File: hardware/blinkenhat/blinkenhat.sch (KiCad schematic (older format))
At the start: 26 parts, among them J1 LED1, J2 LED2, J3 INPUT, J4 Programmer, J5 USB_POWER, J6 GPIO, Q1 2N7002, Q2 2N7002, SW1 RESET, U1 AMS1117-3V3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

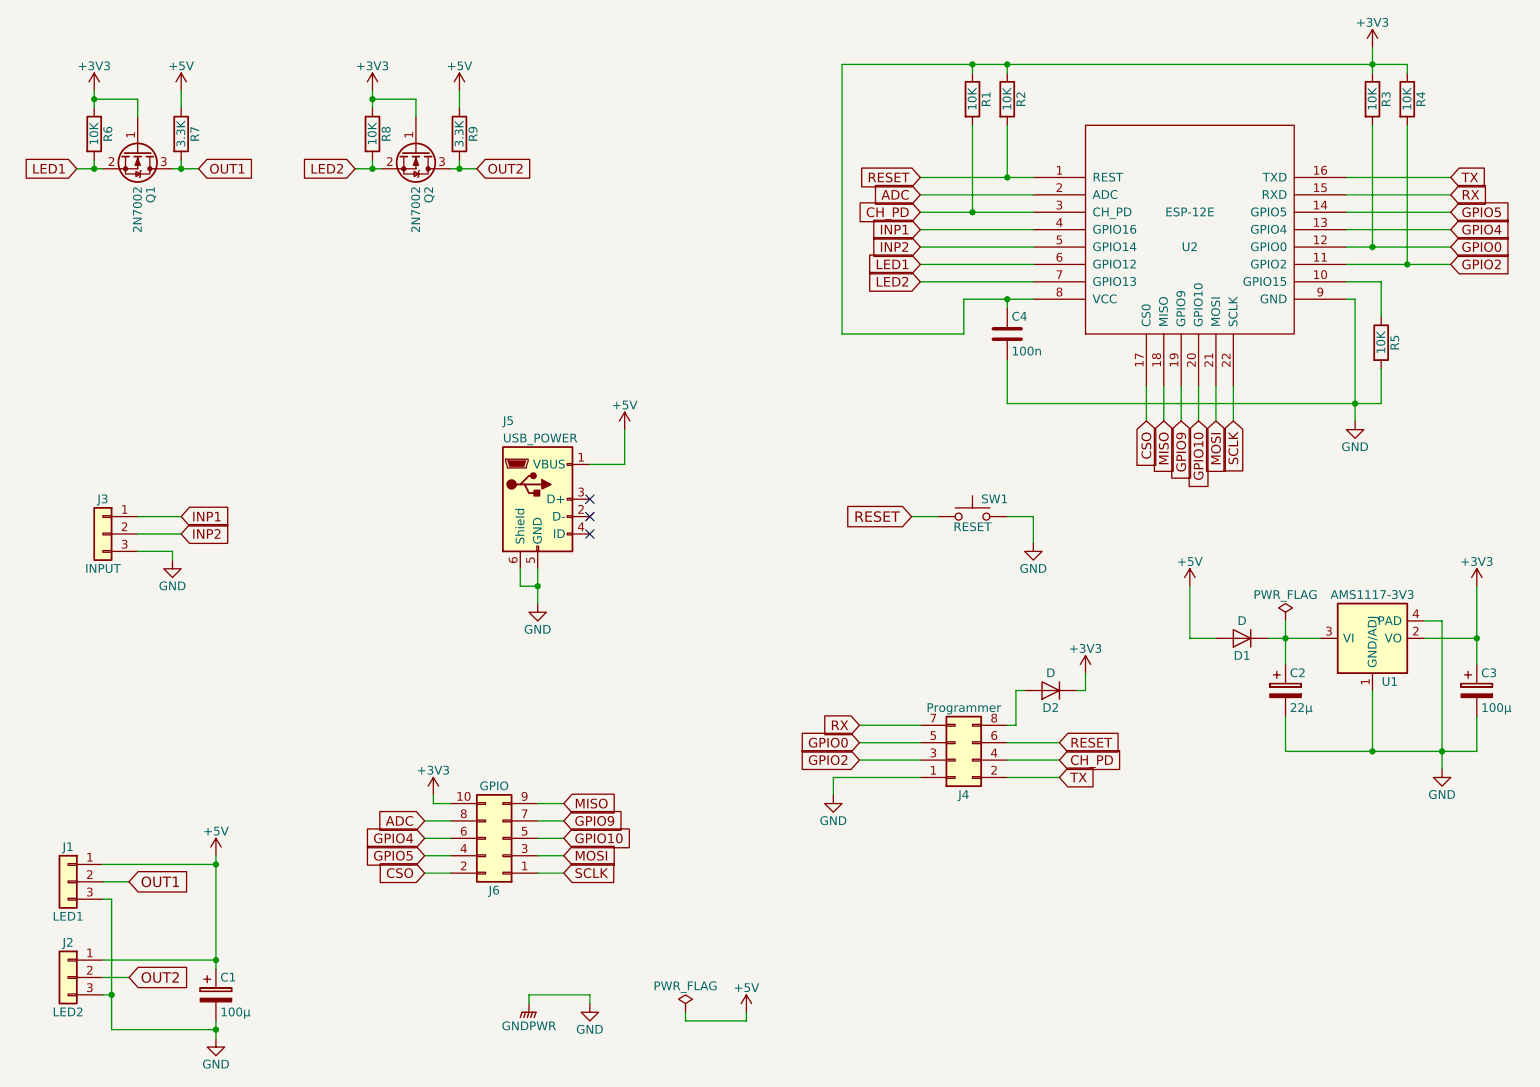
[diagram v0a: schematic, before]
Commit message: Hardware: another schematics update.
Signed-off-by: Jan Losinski <losinski@wh2.tu-dresden.de>
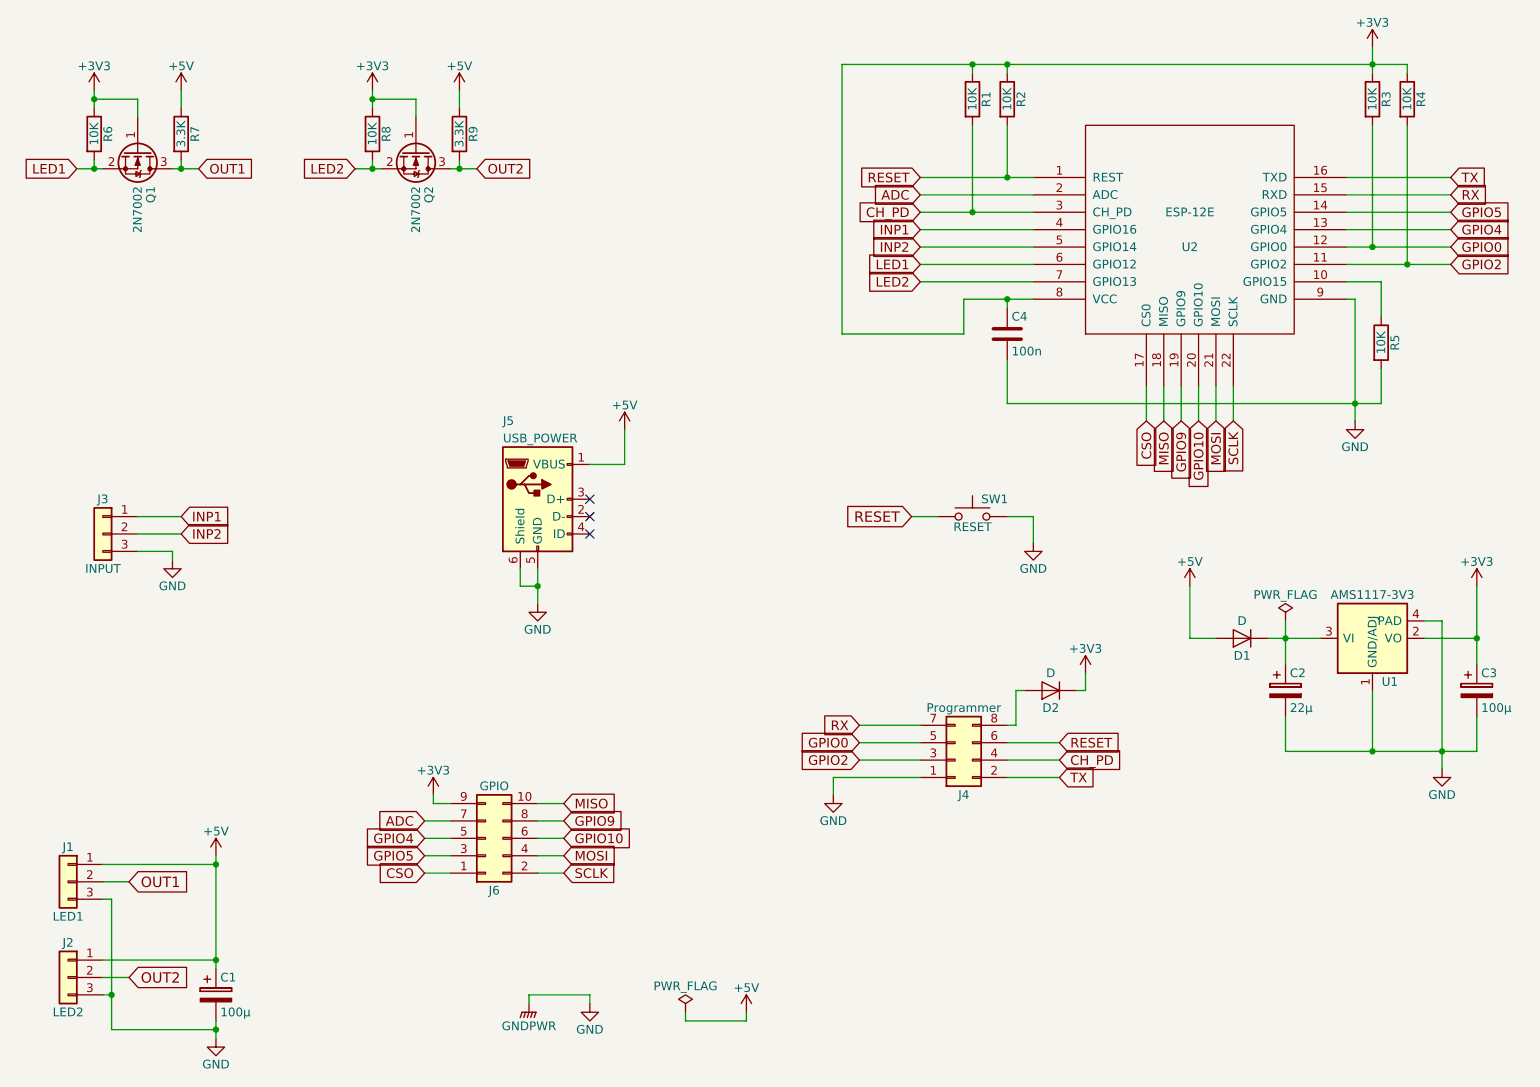
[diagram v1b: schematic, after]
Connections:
- net +3V3: now also J6.9 (Pin_9); no longer J6.10 (Pin_10)
- net ADC: now also J6.7 (Pin_7); no longer J6.8 (Pin_8)
- net CSO: now also J6.1 (Pin_1); no longer J6.2 (Pin_2)
- net GPIO10: now also J6.6 (Pin_6); no longer J6.5 (Pin_5)
- net GPIO4: now also J6.5 (Pin_5); no longer J6.6 (Pin_6)
- net GPIO5: now also J6.3 (Pin_3); no longer J6.4 (Pin_4)
- net GPIO9: now also J6.8 (Pin_8); no longer J6.7 (Pin_7)
- net MISO: now also J6.10 (Pin_10); no longer J6.9 (Pin_9)
- net MOSI: now also J6.4 (Pin_4); no longer J6.3 (Pin_3)
- net SCLK: now also J6.2 (Pin_2); no longer J6.1 (Pin_1)
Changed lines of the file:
@@
 L Conn_02x05_Odd_Even J6
 U 1 1 5A4EBCE1
-P 4300 6000
-F 0 "J6" H 4350 6300 50  0000 C CNN
-F 1 "GPIO" H 4350 5700 50  0000 C CNN
-F 2 "Pin_Headers:Pin_Header_Straight_2x05_Pitch1.27mm" H 4300 6000 50  0001 C CNN
-F 3 "" H 4300 6000 50  0001 C CNN
-	1    4300 6000
-	-1   0    0    1
+P 4200 6000
+F 0 "J6" H 4250 6300 50  0000 C CNN
+F 1 "GPIO" H 4250 5700 50  0000 C CNN
+F 2 "Pin_Headers:Pin_Header_Straight_2x05_Pitch1.27mm" H 4200 6000 50  0001 C CNN
+F 3 "" H 4200 6000 50  0001 C CNN
+	1    4200 6000
+	1    0    0    1
 $EndComp
 Text GLabel 6700 2300 0    55   Input ~ 0
@@
 	9300 5150 9300 5500
 Wire Wire Line
-	9900 4550 9900 5000
+	9900 4550 9900 4850
+Wire Wire Line
+	9900 4850 9900 5000
 Wire Wire Line
 	9900 4850 9600 4850
@@
 	9600 4750 9700 4750
 Wire Wire Line
-	9700 4750 9700 5600
+	9700 4750 9700 5500
+Wire Wire Line
+	9700 5500 9700 5600
 Connection ~ 9300 5500
 Wire Wire Line
 	8800 5300 8800 5500
 Wire Wire Line
-	8800 5500 9900 5500
+	8800 5500 9300 5500
+Wire Wire Line
+	9300 5500 9700 5500
+Wire Wire Line
+	9700 5500 9900 5500
 Connection ~ 8800 4850
 Wire Wire Line
@@
 Connection ~ 9900 4850
 Wire Wire Line
-	4500 4450 4500 4650
+	4500 4450 4500 4550
+Wire Wire Line
+	4500 4550 4500 4650
 Wire Wire Line
 	4500 4550 4400 4550
@@
 	7250 5350 7200 5350
 Wire Wire Line
-	9150 2600 9750 2600
+	9150 2600 9300 2600
+Wire Wire Line
+	9300 2600 9750 2600
 Wire Wire Line
 	9300 2600 9300 1900
@@
 	9500 1900 9500 2700
 Wire Wire Line
-	9150 2700 9750 2700
+	9150 2700 9500 2700
+Wire Wire Line
+	9500 2700 9750 2700
 Wire Wire Line
 	9150 2800 9350 2800
@@
 	9150 2900 9200 2900
 Wire Wire Line
-	9200 2900 9200 3600
+	9200 2900 9200 3500
+Wire Wire Line
+	9200 3500 9200 3600
 Wire Wire Line
 	9350 3500 9350 3300
@@
 	7200 1900 7200 2200
 Wire Wire Line
-	6700 2200 7350 2200
+	6700 2200 7200 2200
+Wire Wire Line
+	7200 2200 7350 2200
 Wire Wire Line
 	7000 1900 7000 2400
 Wire Wire Line
-	6700 2400 7350 2400
+	6700 2400 7000 2400
+Wire Wire Line
+	7000 2400 7350 2400
 Wire Wire Line
 	7000 1600 7000 1550
 Wire Wire Line
-	6250 1550 9500 1550
+	6250 1550 7000 1550
+Wire Wire Line
+	7000 1550 7200 1550
+Wire Wire Line
+	7200 1550 9300 1550
+Wire Wire Line
+	9300 1550 9500 1550
 Wire Wire Line
 	7200 1550 7200 1600
@@
 	6700 2800 7350 2800
 Wire Wire Line
-	6950 2900 7350 2900
+	6950 2900 7200 2900
+Wire Wire Line
+	7200 2900 7350 2900
 Wire Wire Line
 	6950 2900 6950 3100
@@
 	6250 3100 6250 1550
 Wire Wire Line
-	9300 1450 9300 1600
+	9300 1450 9300 1550
+Wire Wire Line
+	9300 1550 9300 1600
 Connection ~ 7200 1550
 Wire Wire Line
@@
 Connection ~ 9300 1550
 Wire Wire Line
-	7200 3500 9350 3500
+	7200 3500 9200 3500
+Wire Wire Line
+	9200 3500 9350 3500
 Wire Wire Line
 	7200 3500 7200 3250
@@
 	2000 6350 2050 6350
 Wire Wire Line
-	2050 6350 2050 7100
-Wire Wire Line
-	2650 6100 2650 6750
+	2050 6350 2050 6900
+Wire Wire Line
+	2050 6900 2050 7100
+Wire Wire Line
+	2650 6100 2650 6150
+Wire Wire Line
+	2650 6150 2650 6700
+Wire Wire Line
+	2650 6700 2650 6750
 Connection ~ 2650 6700
 Wire Wire Line
 	2050 7100 2650 7100
 Wire Wire Line
-	2650 7050 2650 7150
+	2650 7050 2650 7100
+Wire Wire Line
+	2650 7100 2650 7150
 Connection ~ 2050 6900
 Wire Wire Line
@@
 	3550 2100 3550 2150
 Wire Wire Line
-	3450 2150 3600 2150
-Wire Wire Line
-	4000 2150 4150 2150
+	3450 2150 3550 2150
+Wire Wire Line
+	3550 2150 3600 2150
+Wire Wire Line
+	4000 2150 4050 2150
+Wire Wire Line
+	4050 2150 4150 2150
 Wire Wire Line
 	4050 2150 4050 2100
 Wire Wire Line
-	2400 2150 2550 2150
+	2400 2150 2450 2150
+Wire Wire Line
+	2450 2150 2550 2150
 Wire Wire Line
 	2450 2150 2450 2100
@@
 	1950 2100 1950 2150
 Wire Wire Line
-	1850 2150 2000 2150
+	1850 2150 1950 2150
+Wire Wire Line
+	1950 2150 2000 2150
 Wire Wire Line
 	2200 1850 2200 1750
@@
 	2200 1750 1950 1750
 Wire Wire Line
-	1950 1700 1950 1800
+	1950 1700 1950 1750
+Wire Wire Line
+	1950 1750 1950 1800
 Wire Wire Line
 	3800 1850 3800 1750
@@
 	3800 1750 3550 1750
 Wire Wire Line
-	3550 1700 3550 1800
+	3550 1700 3550 1750
+Wire Wire Line
+	3550 1750 3550 1800
 Wire Wire Line
 	4050 1700 4050 1800
@@
 	5700 7050 5700 7000
 Wire Wire Line
-	8800 4750 8800 5000
-Wire Wire Line
-	8700 4850 9000 4850
+	8800 4750 8800 4850
+Wire Wire Line
+	8800 4850 8800 5000
+Wire Wire Line
+	8700 4850 8800 4850
+Wire Wire Line
+	8800 4850 9000 4850
 Wire Wire Line
 	8400 4850 8250 4850
